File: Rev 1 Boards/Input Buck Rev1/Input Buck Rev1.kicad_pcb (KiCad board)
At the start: 2 copper layers, 31 parts, among them J4 Conn_01x02_Socket, Q1 RS1G120MNTB, Q2 RS1G120MNTB, U1 BQ24640

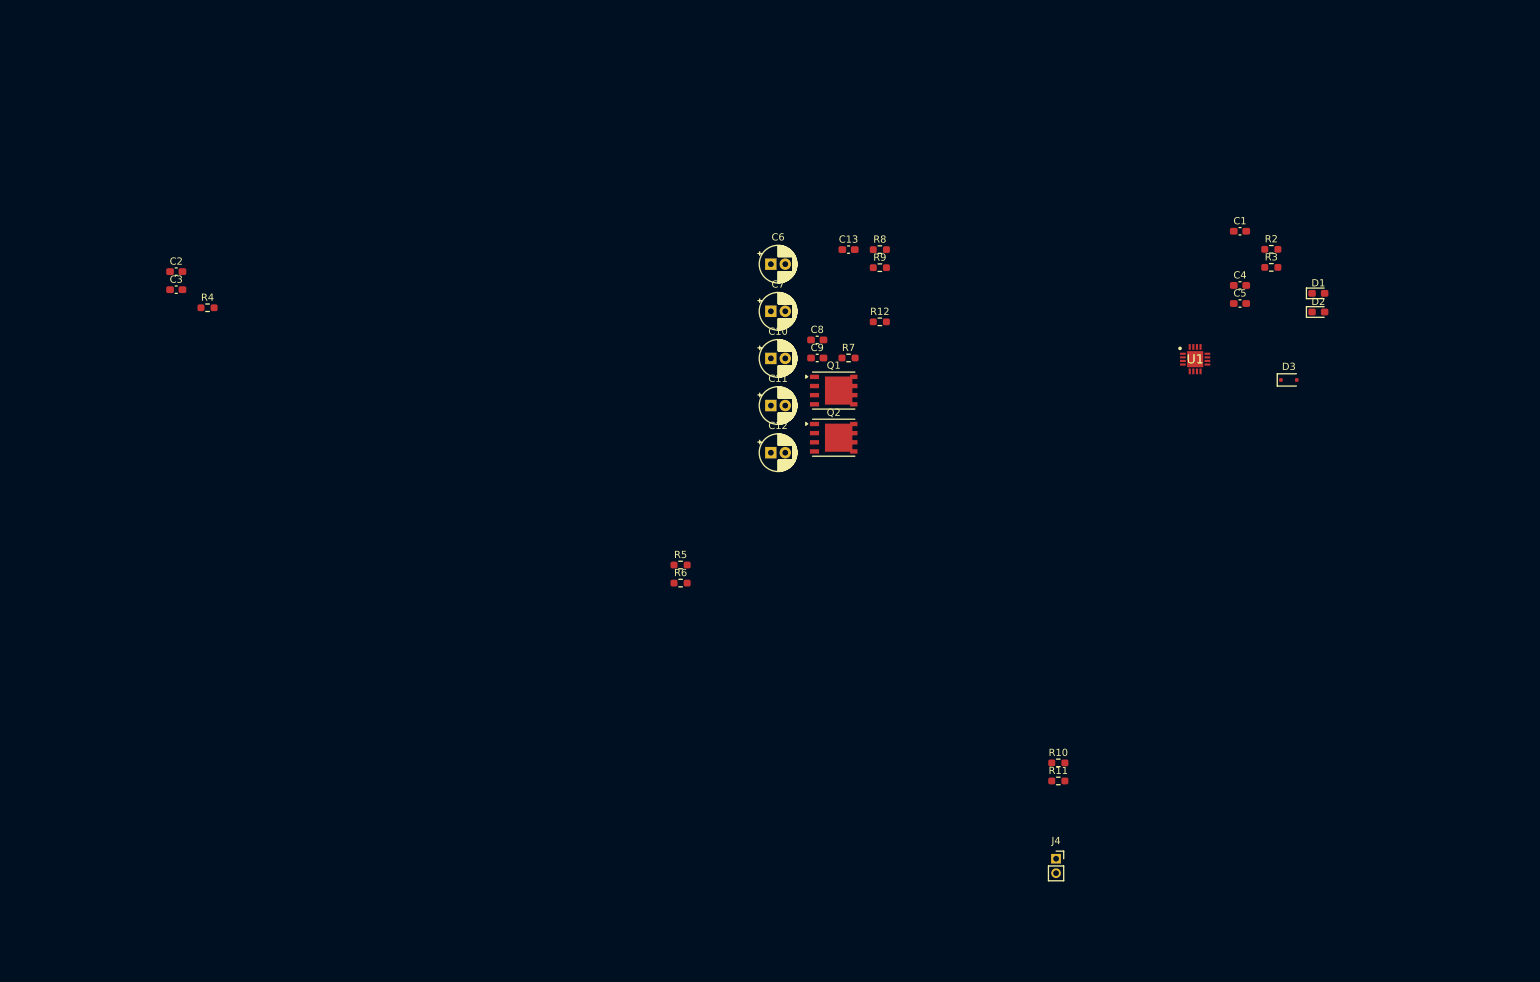
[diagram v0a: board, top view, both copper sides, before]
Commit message: Layout iteration 1 for the input buck
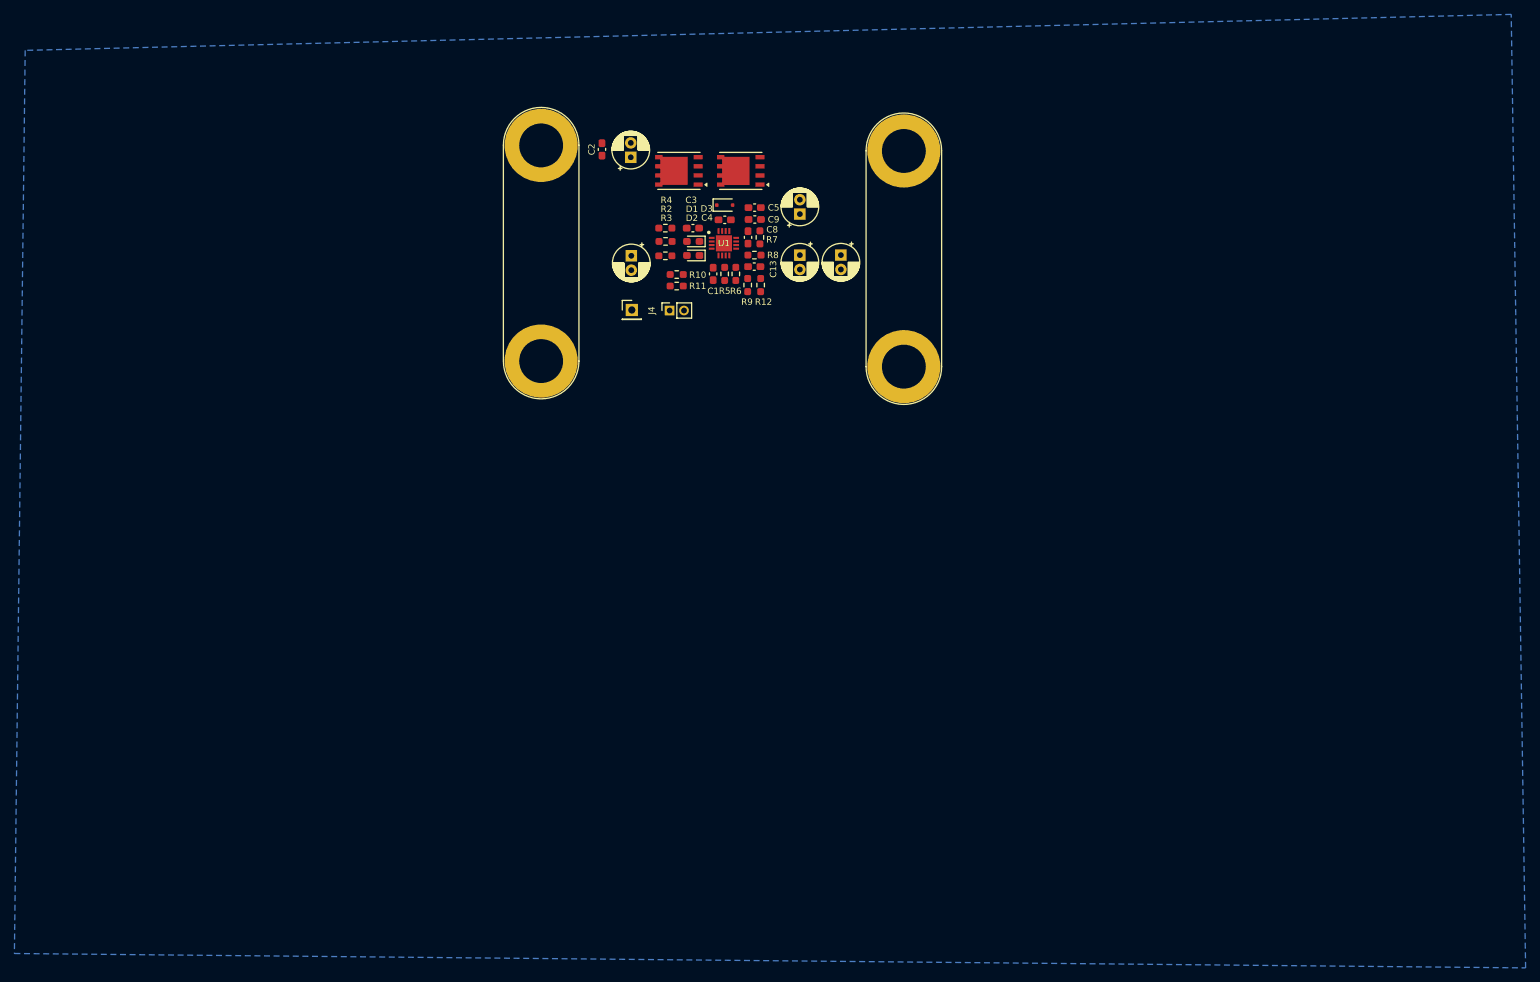
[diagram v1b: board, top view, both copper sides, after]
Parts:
- added J1: Conn_01x02_Socket, Connector:Banana_Jack_2Pin, F.Cu at (160.6, 72.5)
- added J2: Conn_01x02_Socket, Connector:Banana_Jack_2Pin, F.Cu at (110.2, 71.7)
- added J3: Conn_01x01_Pin, Connector_PinHeader_2.54mm:PinHeader_1x01_P2.54mm_Vertical, F.Cu at (122.8, 64.6)
- moved J4 93.2 mm to (128.1, 64.7), turned to 90 degrees
- moved D2 87.2 mm to (131.3, 57.0), turned to 180 degrees
- moved D1 87.2 mm to (131.3, 55.0), turned to 180 degrees
- moved R11 86.8 mm to (129.0, 61.2)
- moved R10 86.1 mm to (129.0, 59.6), turned to 180 degrees
- moved R3 84.2 mm to (127.5, 57.0)
- moved R2 84.2 mm to (127.5, 55.0)
- moved D3 82.1 mm to (135.7, 50.0)
- moved C1 73.4 mm to (134.1, 59.6), turned to -90 degrees
- moved C3 72.3 mm to (131.3, 53.2), turned to 180 degrees
- moved C4 72.2 mm to (135.7, 52.0)
- moved C5 68.8 mm to (139.9, 50.4)
- moved U1 67.4 mm to (135.6, 55.3)
- moved R4 64.6 mm to (127.5, 53.2)
- moved C2 61.5 mm to (118.7, 42.3), turned to 90 degrees
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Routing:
- added copper zone on B.Cu, net GNDPWR

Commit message: Finished layout
Still need to replace the footprint for the inductor
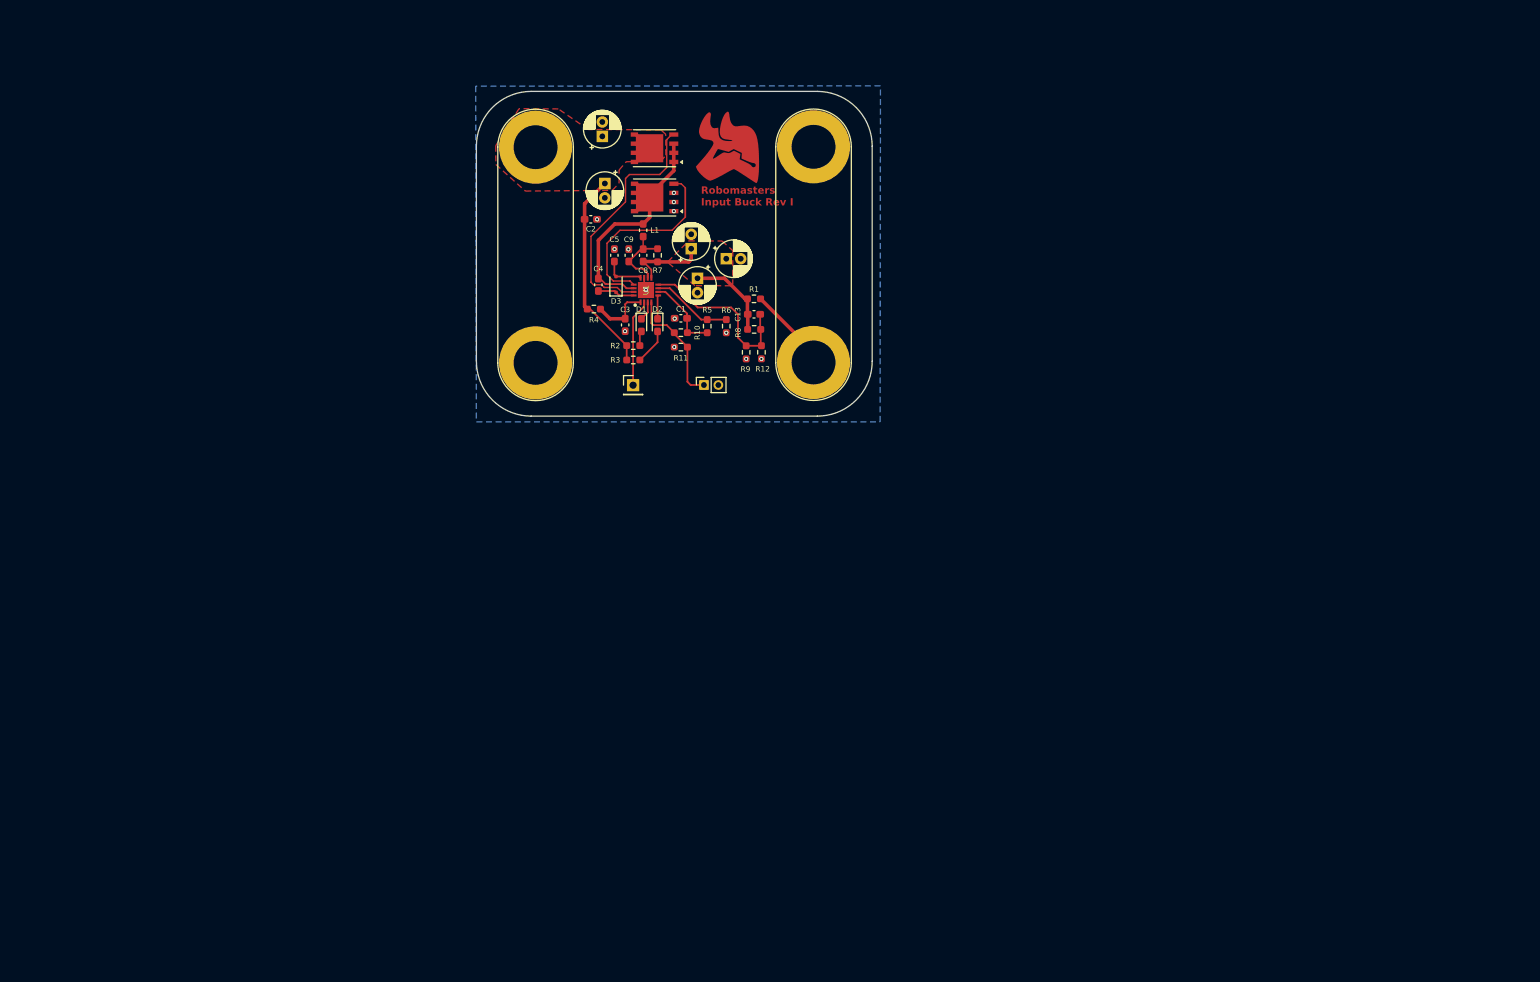
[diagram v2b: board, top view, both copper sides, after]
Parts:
- added G*** (x2): LOGO, LOGO, F.Cu at (136.1, 42.0)
- added L1: 4.7u, Inductor_SMD:L_0603_1608Metric_Pad1.05x0.95mm_HandSolder, F.Cu at (124.4, 53.5)
- added R1: 50, Resistor_SMD:R_0603_1608Metric_Pad0.98x0.95mm_HandSolder, F.Cu at (139.8, 63.0)
- moved J1 33.0 mm to (148.1, 41.9), turned to -90 degrees
- moved C5 20.6 mm to (120.4, 57.0), turned to 90 degrees
- moved C4 19.7 mm to (118.2, 61.1), turned to 90 degrees
- moved D3 18.7 mm to (120.6, 61.0), turned to 90 degrees
- moved C9 18.2 mm to (122.4, 57.0), turned to 90 degrees
- moved C3 16.4 mm to (121.9, 66.7), turned to -90 degrees
- moved C10 15.9 mm to (135.9, 57.5), turned to 0 degrees
- moved C11 15.8 mm to (131.1, 56.1)
- moved R2 15.2 mm to (123.0, 69.5)
- moved R3 15.1 mm to (123.0, 71.5)
- moved R4 15.0 mm to (117.5, 64.5)
- moved C8 14.8 mm to (124.4, 57.0)
- moved C12 14.6 mm to (131.9, 60.2)
- moved R7 14.4 mm to (126.4, 57.0)
- moved D1 13.7 mm to (124.1, 66.7), turned to -90 degrees
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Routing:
- net /Input Buck/PH: track 0.00 -> 41.9 mm
- net /Input Buck/HIDRV: track 0.00 -> 34.4 mm
- net /Input Buck/IN: track 0.00 -> 29.2 mm
- net /Input Buck/LODRV: track 0.00 -> 26.9 mm
- net /Input Buck/VFB: track 0.00 -> 24.2 mm
- net /Input Buck/SRN: track 0.00 -> 23.5 mm
- net /Input Buck/TS: track 0.00 -> 16.8 mm
- net /out: track 0.00 -> 13.6 mm
- net /Input Buck/CHARGE_EN: track 0.00 -> 12.2 mm
- net /Input Buck/SRP: track 0.00 -> 11.6 mm
- net /Input Buck/ISET: track 0.00 -> 11.3 mm
- net /Input Buck/VREF: track 0.00 -> 10.9 mm
- net /Input Buck/VCC: track 0.00 -> 8.27 mm
- net /Input Buck/REGN: track 0.00 -> 5.67 mm
- net /Input Buck/BTST: track 0.00 -> 5.17 mm
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- added copper zone on F.Cu, net /Input Buck/IN
- added copper zone on F.Cu, net /Input Buck/SRN
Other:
- board outline added: 55 x 45.1 mm
- board text added: "Robomasters Input Buck Rev I"

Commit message: Added labels
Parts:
- R1 (50 Ω): renamed from R1
- moved J3 0.78 mm to (123.0, 74.2)
- moved J4 0.78 mm to (132.8, 74.2)
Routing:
- net /Input Buck/TS: track 16.8 -> 14.9 mm
- net /Input Buck/CHARGE_EN: track 12.2 -> 11.4 mm
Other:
- board text added: "CH_EN"
- board text added: "GND"
- board text added: "TS"

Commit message: More labels
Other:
- board text added: "GNDPWR"
- board text added: "IN"
- board text added: "OUT"
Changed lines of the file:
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@@
+		)
+	)
+	(gr_text "IN"
+		(at 108.275 49.625 0)
+		(layer "F.SilkS")
+		(effects
+			(font
+				(size 1.5 1.5)
+				(thickness 0.3)
+				(bold yes)
+			)
+			(justify left bottom)
+		)
+	)
+	(gr_text "GND"
+		(at 145.725 49.575 0)
+		(layer "F.SilkS")
+		(effects
+			(font
+				(size 1.5 1.5)
+				(thickness 0.3)
+				(bold yes)
+			)
+			(justify left bottom)
+		)
+	)
+	(gr_text "GNDPWR"
+		(at 104.725 66.225 0)
+		(layer "F.SilkS")
+		(effects
+			(font
+				(size 1.5 1.5)
+				(thickness 0.3)
+				(bold yes)
+			)
+			(justify left bottom)
 		)
 	)
@@
 		(layer "F.SilkS")
 		(effects
+			(font
+				(size 1.5 1.5)
+				(thickness 0.3)
+				(bold yes)
+			)
+			(justify left bottom)
+		)
+	)
+	(gr_text "OUT"
+		(at 145.85 66.25 0)
+		(layer "F.SilkS")
+		(effects
